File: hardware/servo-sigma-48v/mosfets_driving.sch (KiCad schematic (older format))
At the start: 74 parts, among them Q1 STL160NS3LLH7, Q2 STL160NS3LLH7, Q3 STL160NS3LLH7, Q4 STL160NS3LLH7, Q5 STL160NS3LLH7, Q6 STL160NS3LLH7, U4 L6398, U6 L6398, U7 L6398

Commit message: Finished routing of the servo controller
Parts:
- removed J?: CONN_01X02, Sigmadrone:PhoenixContact_MKDS_02x7.62mm_Vertical, symbol conn:CONN_01X02
- removed R?: 0.0005 1%, Resistors_SMD:R_2512, symbol device:R
- added J7: CONN_01X02, Sigmadrone:PhoenixContact_MKDS_02x7.62mm_Vertical, symbol conn:CONN_01X02
- gave numbers to parts that had none: 18
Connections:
- net labels added: AUX_H, AUX_L, R_ISENSE_N, R_ISENSE_P
- wire segments 247 -> 250

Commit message: Updated the footprints
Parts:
- C16, C18, C21, C23, C33, C35, C48, C49: footprint Capacitors_SMD:C_0603 -> Capacitor_SMD:C_0603_1608Metric; symbol device:C -> servo-sigma-48v-rescue:C-device
- C17, C20, C22, C26, C34, C36, C47, C50: footprint Capacitors_SMD:C_0805 -> Capacitor_SMD:C_0805_2012Metric; symbol device:C -> servo-sigma-48v-rescue:C-device
- D10, D11, D12, D13, D14, D15, D16, D17, D6, D7, D8, D9: symbol device:D_Schottky -> servo-sigma-48v-rescue:D_Schottky-device
- J7: symbol conn:CONN_01X02 -> servo-sigma-48v-rescue:CONN_01X02-conn
- Q1, Q2, Q3, Q4, Q5, Q6, Q7, Q8: symbol device:Q_NMOS_SGD -> servo-sigma-48v-rescue:Q_NMOS_SGD-device
- R18, R22, R23, R24, R25, R26, R27, R29, R32, R33, R34, R35, R36, R37, R39, R42, R43, R53, R54, R55, R56, R74, R75, R76, R77, R78, R79, R80: footprint Resistors_SMD:R_0603 -> Resistor_SMD:R_0603_1608Metric; symbol device:R -> servo-sigma-48v-rescue:R-device
- R67, R68, R69, R82: footprint Resistors_SMD:R_2512 -> Resistor_SMD:R_2512_6332Metric; symbol device:R -> servo-sigma-48v-rescue:R-device
- U11, U4, U6, U7: footprint Housings_SOIC:SOIC-8_3.9x4.9mm_Pitch1.27mm -> Package_SO:SOIC-8_3.9x4.9mm_P1.27mm

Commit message: Work on sigmadrive 2.0
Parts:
- R67, R68, R69, R82: value 0.0005 1% -> 0.010 1%; Part 696-1183-1-ND -> CRA2512-FZ-R010ELFCT-ND
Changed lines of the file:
@@
 P 2750 5700
 F 0 "R67" V 2830 5700 50  0000 C CNN
-F 1 "0.0005 1%" V 2650 5700 50  0000 C CNN
+F 1 "0.010 1%" V 2650 5700 50  0000 C CNN
 F 2 "Resistor_SMD:R_2512_6332Metric" V 2680 5700 50  0001 C CNN
 F 3 "http://www.yageo.com.tw/exep/pages/download/literatures/PYu-R_INT-thick_7.pdf" H 2750 5700 50  0001 C CNN
-F 4 "696-1183-1-ND" V 2750 5700 60  0001 C CNN "Part"
+F 4 "CRA2512-FZ-R010ELFCT-ND" V 2750 5700 60  0001 C CNN "Part"
 F 5 "DigiKey" V 2750 5700 60  0001 C CNN "Provider"
 	1    2750 5700
@@
 P 6100 5700
 F 0 "R68" V 6180 5700 50  0000 C CNN
-F 1 "0.0005 1%" V 6000 5700 50  0000 C CNN
+F 1 "0.010 1%" V 6000 5700 50  0000 C CNN
 F 2 "Resistor_SMD:R_2512_6332Metric" V 6030 5700 50  0001 C CNN
 F 3 "http://www.yageo.com.tw/exep/pages/download/literatures/PYu-R_INT-thick_7.pdf" H 6100 5700 50  0001 C CNN
-F 4 "696-1183-1-ND" V 6100 5700 60  0001 C CNN "Part"
+F 4 "CRA2512-FZ-R010ELFCT-ND" V 6100 5700 60  0001 C CNN "Part"
 F 5 "DigiKey" V 6100 5700 60  0001 C CNN "Provider"
 	1    6100 5700
@@
 P 9600 5700
 F 0 "R69" V 9680 5700 50  0000 C CNN
-F 1 "0.0005 1%" V 9500 5700 50  0000 C CNN
+F 1 "0.010 1%" V 9500 5700 50  0000 C CNN
 F 2 "Resistor_SMD:R_2512_6332Metric" V 9530 5700 50  0001 C CNN
 F 3 "http://www.yageo.com.tw/exep/pages/download/literatures/PYu-R_INT-thick_7.pdf" H 9600 5700 50  0001 C CNN
-F 4 "696-1183-1-ND" V 9600 5700 60  0001 C CNN "Part"
+F 4 "CRA2512-FZ-R010ELFCT-ND" V 9600 5700 60  0001 C CNN "Part"
 F 5 "DigiKey" V 9600 5700 60  0001 C CNN "Provider"
 	1    9600 5700
@@
 	1    0    0    -1
 $EndComp
-Connection ~ 14550 6100
-Wire Wire Line
-	14550 6100 14550 6200
-$Comp
-L servo-sigma-48v-rescue:R-device R82
-U 1 1 5BCAB8A5
-P 14550 5700
-F 0 "R82" V 14630 5700 50  0000 C CNN
-F 1 "0.0005 1%" V 14450 5700 50  0000 C CNN
-F 2 "Resistor_SMD:R_2512_6332Metric" V 14480 5700 50  0001 C CNN
-F 3 "http://www.yageo.com.tw/exep/pages/download/literatures/PYu-R_INT-thick_7.pdf" H 14550 5700 50  0001 C CNN
-F 4 "696-1183-1-ND" V 14550 5700 60  0001 C CNN "Part"
-F 5 "DigiKey" V 14550 5700 60  0001 C CNN "Provider"
-	1    14550 5700
-	1    0    0    -1
-$EndComp
-Wire Wire Line
-	14550 5850 14550 6100
-Text HLabel 14950 5400 2    60   Output ~ 0
-R_ISENSE_P
-Text HLabel 14950 6100 2    60   Output ~ 0
-R_ISENSE_N
-Wire Wire Line
-	14950 5400 14550 5400
-Connection ~ 14550 5400
-Wire Wire Line
-	14550 5400 14550 5550
-Wire Wire Line
-	14950 6100 14550 6100
 Wire Wire Line
 	13550 5250 13550 6100
@@
 Wire Wire Line
 	14550 4750 14900 4750
+Text HLabel 14950 5400 2    60   Output ~ 0
+R_ISENSE_P
+Text HLabel 14950 6100 2    60   Output ~ 0
+R_ISENSE_N
+Wire Wire Line
+	14550 5850 14550 6100
+Wire Wire Line
+	14550 6100 14550 6200
+Connection ~ 14550 6100
+Wire Wire Line
+	14950 6100 14550 6100
 Wire Wire Line
 	14550 4750 14550 5400
+Wire Wire Line
+	14550 5400 14550 5550
+Connection ~ 14550 5400
+Wire Wire Line
+	14950 5400 14550 5400
+$Comp
+L servo-sigma-48v-rescue:R-device R82
+U 1 1 5BCAB8A5
+P 14550 5700
+F 0 "R82" V 14630 5700 50  0000 C CNN
+F 1 "0.010 1%" V 14450 5700 50  0000 C CNN
+F 2 "Resistor_SMD:R_2512_6332Metric" V 14480 5700 50  0001 C CNN
+F 3 "http://www.yageo.com.tw/exep/pages/download/literatures/PYu-R_INT-thick_7.pdf" H 14550 5700 50  0001 C CNN
+F 4 "CRA2512-FZ-R010ELFCT-ND" V 14550 5700 60  0001 C CNN "Part"
+F 5 "DigiKey" V 14550 5700 60  0001 C CNN "Provider"
+	1    14550 5700
+	1    0    0    -1
+$EndComp
 $EndSCHEMATC

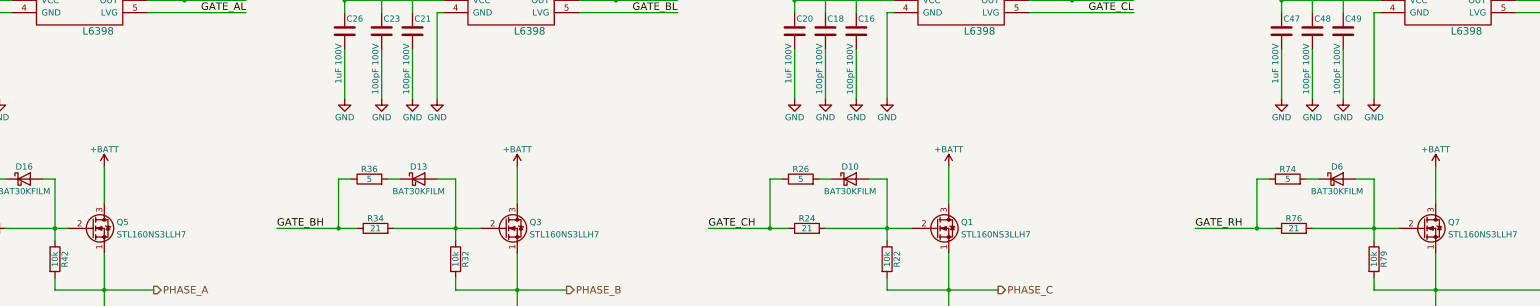
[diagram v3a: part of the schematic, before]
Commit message: Changed the MCU to use 100 pin
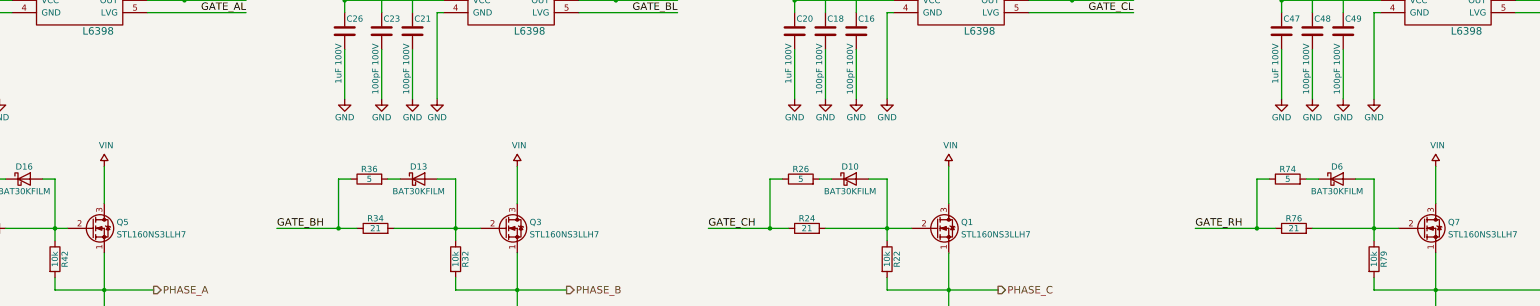
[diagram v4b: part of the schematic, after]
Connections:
- net +BATT renamed VIN
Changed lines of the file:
@@
-$EndComp
-$Comp
-L power:+BATT #PWR026
-U 1 1 58BF9644
-P 2750 3300
-F 0 "#PWR026" H 2750 3150 50  0001 C CNN
-F 1 "+BATT" H 2750 3440 50  0000 C CNN
-F 2 "" H 2750 3300 50  0001 C CNN
-F 3 "" H 2750 3300 50  0001 C CNN
-	1    2750 3300
-	1    0    0    -1
 $EndComp
 $Comp
@@
 GATE_BH
 $Comp
-L power:+BATT #PWR028
-U 1 1 58C227E1
-P 6100 3300
-F 0 "#PWR028" H 6100 3150 50  0001 C CNN
-F 1 "+BATT" H 6100 3440 50  0000 C CNN
-F 2 "" H 6100 3300 50  0001 C CNN
-F 3 "" H 6100 3300 50  0001 C CNN
-	1    6100 3300
-	1    0    0    -1
-$EndComp
-$Comp
 L power:GND #PWR029
 U 1 1 58C227F2
@@
 Text HLabel 6500 4300 2    60   Output ~ 0
 PHASE_B
-$Comp
-L power:+BATT #PWR030
-U 1 1 58C22F7A
-P 9600 3300
-F 0 "#PWR030" H 9600 3150 50  0001 C CNN
-F 1 "+BATT" H 9600 3440 50  0000 C CNN
-F 2 "" H 9600 3300 50  0001 C CNN
-F 3 "" H 9600 3300 50  0001 C CNN
-	1    9600 3300
-	1    0    0    -1
-$EndComp
 $Comp
 L power:GND #PWR031
@@
 Wire Wire Line
 	6100 5350 6100 5550
-$Comp
-L power:+BATT #PWR069
-U 1 1 5BC7FFE0
-P 13550 3300
-F 0 "#PWR069" H 13550 3150 50  0001 C CNN
-F 1 "+BATT" H 13550 3440 50  0000 C CNN
-F 2 "" H 13550 3300 50  0001 C CNN
-F 3 "" H 13550 3300 50  0001 C CNN
-	1    13550 3300
-	1    0    0    -1
-$EndComp
 $Comp
 L power:GND #PWR070
@@
 	1    0    0    -1
 $EndComp
+$Comp
+L sigmadrone:VIN #PWR?
+U 1 1 5D199B5E
+P 13550 3300
+AR Path="/58BE27E6/5D199B5E" Ref="#PWR?"  Part="1"
+AR Path="/58BF664D/5D199B5E" Ref="#PWR0129"  Part="1"
+F 0 "#PWR0129" H 13550 3150 50  0001 C CNN
+F 1 "VIN" H 13565 3473 50  0000 C CNN
+F 2 "" H 13550 3300 50  0000 C CNN
+F 3 "" H 13550 3300 50  0000 C CNN
+	1    13550 3300
+	1    0    0    -1
+$EndComp
+$Comp
+L sigmadrone:VIN #PWR?
+U 1 1 5D1A8822
+P 9600 3300
+AR Path="/58BE27E6/5D1A8822" Ref="#PWR?"  Part="1"
+AR Path="/58BF664D/5D1A8822" Ref="#PWR0130"  Part="1"
+F 0 "#PWR0130" H 9600 3150 50  0001 C CNN
+F 1 "VIN" H 9615 3473 50  0000 C CNN
+F 2 "" H 9600 3300 50  0000 C CNN
+F 3 "" H 9600 3300 50  0000 C CNN
+	1    9600 3300
+	1    0    0    -1
+$EndComp
+$Comp
+L sigmadrone:VIN #PWR?
+U 1 1 5D1B74E6
+P 6100 3300
+AR Path="/58BE27E6/5D1B74E6" Ref="#PWR?"  Part="1"
+AR Path="/58BF664D/5D1B74E6" Ref="#PWR0131"  Part="1"
+F 0 "#PWR0131" H 6100 3150 50  0001 C CNN
+F 1 "VIN" H 6115 3473 50  0000 C CNN
+F 2 "" H 6100 3300 50  0000 C CNN
+F 3 "" H 6100 3300 50  0000 C CNN
+	1    6100 3300
+	1    0    0    -1
+$EndComp
+$Comp
+L sigmadrone:VIN #PWR?
+U 1 1 5D1C61AA
+P 2750 3300
+AR Path="/58BE27E6/5D1C61AA" Ref="#PWR?"  Part="1"
+AR Path="/58BF664D/5D1C61AA" Ref="#PWR0132"  Part="1"
+F 0 "#PWR0132" H 2750 3150 50  0001 C CNN
+F 1 "VIN" H 2765 3473 50  0000 C CNN
+F 2 "" H 2750 3300 50  0000 C CNN
+F 3 "" H 2750 3300 50  0000 C CNN
+	1    2750 3300
+	1    0    0    -1
+$EndComp

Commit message: Work on verson 2.0
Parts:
- Q1, Q2, Q3, Q4, Q5, Q6, Q7, Q8: Value1 (none) -> STL160N4F7
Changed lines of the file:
@@
 GATE_AH
-$Comp
-L servo-sigma-48v-rescue:Q_NMOS_SGD-device Q3
-U 1 1 58BF7288
-P 6000 3800
-F 0 "Q3" H 6200 3850 50  0000 L CNN
-F 1 "STL160NS3LLH7" H 6200 3750 50  0000 L CNN
-F 2 "Sigmadrone:PQFN_5x6_SGD" H 6200 3900 50  0001 C CNN
-F 3 "http://www.st.com/content/ccc/resource/technical/document/datasheet/6c/2c/68/6d/40/eb/44/cd/DM00087549.pdf/files/DM00087549.pdf/jcr:content/translations/en.DM00087549.pdf" H 6000 3800 50  0001 C CNN
-F 4 "DigiKey" H 6000 3800 60  0001 C CNN "Provider"
-F 5 "497-14988-6-ND" H 6000 3800 60  0001 C CNN "Part"
-	1    6000 3800
-	1    0    0    -1
-$EndComp
 $Comp
 L power:GND #PWR027
@@
 	8150 5050 8300 5050
 $Comp
-L servo-sigma-48v-rescue:Q_NMOS_SGD-device Q6
-U 1 1 5A8C12F1
-P 2650 5050
-F 0 "Q6" H 2850 5100 50  0000 L CNN
-F 1 "STL160NS3LLH7" H 2850 5000 50  0000 L CNN
-F 2 "Sigmadrone:PQFN_5x6_SGD" H 2850 5150 50  0001 C CNN
-F 3 "http://www.st.com/content/ccc/resource/technical/document/datasheet/6c/2c/68/6d/40/eb/44/cd/DM00087549.pdf/files/DM00087549.pdf/jcr:content/translations/en.DM00087549.pdf" H 2650 5050 50  0001 C CNN
-F 4 "DigiKey" H 2650 5050 60  0001 C CNN "Provider"
-F 5 "497-14988-6-ND" H 2650 5050 60  0001 C CNN "Part"
-	1    2650 5050
-	1    0    0    -1
-$EndComp
-$Comp
-L servo-sigma-48v-rescue:Q_NMOS_SGD-device Q4
-U 1 1 5A8D4DE7
-P 6000 5050
-F 0 "Q4" H 6200 5100 50  0000 L CNN
-F 1 "STL160NS3LLH7" H 6200 5000 50  0000 L CNN
-F 2 "Sigmadrone:PQFN_5x6_SGD" H 6200 5150 50  0001 C CNN
-F 3 "http://www.st.com/content/ccc/resource/technical/document/datasheet/6c/2c/68/6d/40/eb/44/cd/DM00087549.pdf/files/DM00087549.pdf/jcr:content/translations/en.DM00087549.pdf" H 6000 5050 50  0001 C CNN
-F 4 "DigiKey" H 6000 5050 60  0001 C CNN "Provider"
-F 5 "497-14988-6-ND" H 6000 5050 60  0001 C CNN "Part"
-	1    6000 5050
-	1    0    0    -1
-$EndComp
-$Comp
-L servo-sigma-48v-rescue:Q_NMOS_SGD-device Q1
-U 1 1 5A8D51CA
-P 9500 3800
-F 0 "Q1" H 9700 3850 50  0000 L CNN
-F 1 "STL160NS3LLH7" H 9700 3750 50  0000 L CNN
-F 2 "Sigmadrone:PQFN_5x6_SGD" H 9700 3900 50  0001 C CNN
-F 3 "http://www.st.com/content/ccc/resource/technical/document/datasheet/6c/2c/68/6d/40/eb/44/cd/DM00087549.pdf/files/DM00087549.pdf/jcr:content/translations/en.DM00087549.pdf" H 9500 3800 50  0001 C CNN
-F 4 "DigiKey" H 9500 3800 60  0001 C CNN "Provider"
-F 5 "497-14988-6-ND" H 9500 3800 60  0001 C CNN "Part"
-	1    9500 3800
-	1    0    0    -1
-$EndComp
-$Comp
-L servo-sigma-48v-rescue:Q_NMOS_SGD-device Q2
-U 1 1 5A8D529E
-P 9500 5050
-F 0 "Q2" H 9700 5100 50  0000 L CNN
-F 1 "STL160NS3LLH7" H 9700 5000 50  0000 L CNN
-F 2 "Sigmadrone:PQFN_5x6_SGD" H 9700 5150 50  0001 C CNN
-F 3 "http://www.st.com/content/ccc/resource/technical/document/datasheet/6c/2c/68/6d/40/eb/44/cd/DM00087549.pdf/files/DM00087549.pdf/jcr:content/translations/en.DM00087549.pdf" H 9500 5050 50  0001 C CNN
-F 4 "DigiKey" H 9500 5050 60  0001 C CNN "Provider"
-F 5 "497-14988-6-ND" H 9500 5050 60  0001 C CNN "Part"
-	1    9500 5050
-	1    0    0    -1
-$EndComp
-$Comp
 L servo-sigma-48v-rescue:Q_NMOS_SGD-device Q5
 U 1 1 5A928DF8
@@
 F 4 "DigiKey" H 2650 3800 60  0001 C CNN "Provider"
 F 5 "497-14988-6-ND" H 2650 3800 60  0001 C CNN "Part"
+F 6 "STL160N4F7" H 2650 3800 50  0001 C CNN "Value1"
 	1    2650 3800
 	1    0    0    -1
@@
 	9600 5400 9600 5550
 Wire Wire Line
-	10000 6100 9600 6100
-Wire Wire Line
 	6500 6100 6100 6100
-Wire Wire Line
-	3150 6100 2750 6100
 Wire Wire Line
 	3150 5400 2750 5400
@@
 Wire Wire Line
 	12100 5050 12250 5050
-$Comp
-L servo-sigma-48v-rescue:Q_NMOS_SGD-device Q7
-U 1 1 5BC800CA
-P 13450 3800
-F 0 "Q7" H 13650 3850 50  0000 L CNN
-F 1 "STL160NS3LLH7" H 13650 3750 50  0000 L CNN
-F 2 "Sigmadrone:PQFN_5x6_SGD" H 13650 3900 50  0001 C CNN
-F 3 "http://www.st.com/content/ccc/resource/technical/document/datasheet/6c/2c/68/6d/40/eb/44/cd/DM00087549.pdf/files/DM00087549.pdf/jcr:content/translations/en.DM00087549.pdf" H 13450 3800 50  0001 C CNN
-F 4 "DigiKey" H 13450 3800 60  0001 C CNN "Provider"
-F 5 "497-14988-6-ND" H 13450 3800 60  0001 C CNN "Part"
-	1    13450 3800
-	1    0    0    -1
-$EndComp
-$Comp
-L servo-sigma-48v-rescue:Q_NMOS_SGD-device Q8
-U 1 1 5BC800D2
-P 13450 5050
-F 0 "Q8" H 13650 5100 50  0000 L CNN
-F 1 "STL160NS3LLH7" H 13650 5000 50  0000 L CNN
-F 2 "Sigmadrone:PQFN_5x6_SGD" H 13650 5150 50  0001 C CNN
-F 3 "http://www.st.com/content/ccc/resource/technical/document/datasheet/6c/2c/68/6d/40/eb/44/cd/DM00087549.pdf/files/DM00087549.pdf/jcr:content/translations/en.DM00087549.pdf" H 13450 5050 50  0001 C CNN
-F 4 "DigiKey" H 13450 5050 60  0001 C CNN "Provider"
-F 5 "497-14988-6-ND" H 13450 5050 60  0001 C CNN "Part"
-	1    13450 5050
-	1    0    0    -1
-$EndComp
 Wire Wire Line
 	13550 4300 14550 4300
@@
 R_ISENSE_N
 Wire Wire Line
-	14550 5850 14550 6100
-Wire Wire Line
-	14550 6100 14550 6200
-Connection ~ 14550 6100
-Wire Wire Line
-	14950 6100 14550 6100
-Wire Wire Line
 	14550 4750 14550 5400
 Wire Wire Line
@@
 	1    0    0    -1
 $EndComp
+Wire Wire Line
+	14550 6100 14550 6200
+Wire Wire Line
+	14550 5850 14550 6100
+Connection ~ 14550 6100
+Wire Wire Line
+	14950 6100 14550 6100
+Wire Wire Line
+	10000 6100 9600 6100
+Wire Wire Line
+	3150 6100 2750 6100
+$Comp
+L servo-sigma-48v-rescue:Q_NMOS_SGD-device Q6
+U 1 1 5C792FA5
+P 2650 5050
+F 0 "Q6" H 2850 5100 50  0000 L CNN
+F 1 "STL160NS3LLH7" H 2850 5000 50  0000 L CNN
+F 2 "Sigmadrone:PQFN_5x6_SGD" H 2850 5150 50  0001 C CNN
+F 3 "http://www.st.com/content/ccc/resource/technical/document/datasheet/6c/2c/68/6d/40/eb/44/cd/DM00087549.pdf/files/DM00087549.pdf/jcr:content/translations/en.DM00087549.pdf" H 2650 5050 50  0001 C CNN
+F 4 "DigiKey" H 2650 5050 60  0001 C CNN "Provider"
+F 5 "497-14988-6-ND" H 2650 5050 60  0001 C CNN "Part"
+F 6 "STL160N4F7" H 2650 5050 50  0001 C CNN "Value1"
+	1    2650 5050
+	1    0    0    -1
+$EndComp
+$Comp
+L servo-sigma-48v-rescue:Q_NMOS_SGD-device Q3
+U 1 1 5C79432A
+P 6000 3800
+F 0 "Q3" H 6200 3850 50  0000 L CNN
+F 1 "STL160NS3LLH7" H 6200 3750 50  0000 L CNN
+F 2 "Sigmadrone:PQFN_5x6_SGD" H 6200 3900 50  0001 C CNN
+F 3 "http://www.st.com/content/ccc/resource/technical/document/datasheet/6c/2c/68/6d/40/eb/44/cd/DM00087549.pdf/files/DM00087549.pdf/jcr:content/translations/en.DM00087549.pdf" H 6000 3800 50  0001 C CNN
+F 4 "DigiKey" H 6000 3800 60  0001 C CNN "Provider"
+F 5 "497-14988-6-ND" H 6000 3800 60  0001 C CNN "Part"
+F 6 "STL160N4F7" H 6000 3800 50  0001 C CNN "Value1"
+	1    6000 3800
+	1    0    0    -1
+$EndComp
+$Comp
+L servo-sigma-48v-rescue:Q_NMOS_SGD-device Q4
+U 1 1 5C794408
+P 6000 5050
+F 0 "Q4" H 6200 5100 50  0000 L CNN
+F 1 "STL160NS3LLH7" H 6200 5000 50  0000 L CNN
+F 2 "Sigmadrone:PQFN_5x6_SGD" H 6200 5150 50  0001 C CNN
+F 3 "http://www.st.com/content/ccc/resource/technical/document/datasheet/6c/2c/68/6d/40/eb/44/cd/DM00087549.pdf/files/DM00087549.pdf/jcr:content/translations/en.DM00087549.pdf" H 6000 5050 50  0001 C CNN
+F 4 "DigiKey" H 6000 5050 60  0001 C CNN "Provider"
+F 5 "497-14988-6-ND" H 6000 5050 60  0001 C CNN "Part"
+F 6 "STL160N4F7" H 6000 5050 50  0001 C CNN "Value1"
+	1    6000 5050
+	1    0    0    -1
+$EndComp
+$Comp
+L servo-sigma-48v-rescue:Q_NMOS_SGD-device Q1
+U 1 1 5C794DDD
+P 9500 3800
+F 0 "Q1" H 9700 3850 50  0000 L CNN
+F 1 "STL160NS3LLH7" H 9700 3750 50  0000 L CNN
+F 2 "Sigmadrone:PQFN_5x6_SGD" H 9700 3900 50  0001 C CNN
+F 3 "http://www.st.com/content/ccc/resource/technical/document/datasheet/6c/2c/68/6d/40/eb/44/cd/DM00087549.pdf/files/DM00087549.pdf/jcr:content/translations/en.DM00087549.pdf" H 9500 3800 50  0001 C CNN
+F 4 "DigiKey" H 9500 3800 60  0001 C CNN "Provider"
+F 5 "497-14988-6-ND" H 9500 3800 60  0001 C CNN "Part"
+F 6 "STL160N4F7" H 9500 3800 50  0001 C CNN "Value1"
+	1    9500 3800
+	1    0    0    -1
+$EndComp
+$Comp
+L servo-sigma-48v-rescue:Q_NMOS_SGD-device Q2
+U 1 1 5C794EBD
+P 9500 5050
+F 0 "Q2" H 9700 5100 50  0000 L CNN
+F 1 "STL160NS3LLH7" H 9700 5000 50  0000 L CNN
+F 2 "Sigmadrone:PQFN_5x6_SGD" H 9700 5150 50  0001 C CNN
+F 3 "http://www.st.com/content/ccc/resource/technical/document/datasheet/6c/2c/68/6d/40/eb/44/cd/DM00087549.pdf/files/DM00087549.pdf/jcr:content/translations/en.DM00087549.pdf" H 9500 5050 50  0001 C CNN
+F 4 "DigiKey" H 9500 5050 60  0001 C CNN "Provider"
+F 5 "497-14988-6-ND" H 9500 5050 60  0001 C CNN "Part"
+F 6 "STL160N4F7" H 9500 5050 50  0001 C CNN "Value1"
+	1    9500 5050
+	1    0    0    -1
+$EndComp
+$Comp
+L servo-sigma-48v-rescue:Q_NMOS_SGD-device Q7
+U 1 1 5C79539C
+P 13450 3800
+F 0 "Q7" H 13650 3850 50  0000 L CNN
+F 1 "STL160NS3LLH7" H 13650 3750 50  0000 L CNN
+F 2 "Sigmadrone:PQFN_5x6_SGD" H 13650 3900 50  0001 C CNN
+F 3 "http://www.st.com/content/ccc/resource/technical/document/datasheet/6c/2c/68/6d/40/eb/44/cd/DM00087549.pdf/files/DM00087549.pdf/jcr:content/translations/en.DM00087549.pdf" H 13450 3800 50  0001 C CNN
+F 4 "DigiKey" H 13450 3800 60  0001 C CNN "Provider"
+F 5 "497-14988-6-ND" H 13450 3800 60  0001 C CNN "Part"
+F 6 "STL160N4F7" H 13450 3800 50  0001 C CNN "Value1"
+	1    13450 3800
+	1    0    0    -1
+$EndComp
+$Comp
+L servo-sigma-48v-rescue:Q_NMOS_SGD-device Q8
+U 1 1 5C795574
+P 13450 5050
+F 0 "Q8" H 13650 5100 50  0000 L CNN
+F 1 "STL160NS3LLH7" H 13650 5000 50  0000 L CNN
+F 2 "Sigmadrone:PQFN_5x6_SGD" H 13650 5150 50  0001 C CNN
+F 3 "http://www.st.com/content/ccc/resource/technical/document/datasheet/6c/2c/68/6d/40/eb/44/cd/DM00087549.pdf/files/DM00087549.pdf/jcr:content/translations/en.DM00087549.pdf" H 13450 5050 50  0001 C CNN
+F 4 "DigiKey" H 13450 5050 60  0001 C CNN "Provider"
+F 5 "497-14988-6-ND" H 13450 5050 60  0001 C CNN "Part"
+F 6 "STL160N4F7" H 13450 5050 50  0001 C CNN "Value1"
+	1    13450 5050
+	1    0    0    -1
+$EndComp
